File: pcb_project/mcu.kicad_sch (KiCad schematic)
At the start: 0 parts

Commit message: Initial MCU schematic
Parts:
- added C28: 4.7μF, symbol Device:C
- added C29, C32: 1μF, symbol Device:C
- added C30, C31, C33, C35, C36, C37, C38, C39: 100nF, symbol Device:C
- added C34, C41: 10pF, symbol Device:C
- added C40: 10μF, symbol Device:C
- added J3: Conn_ST_STDC14, symbol Connector:Conn_ST_STDC14
- added R46, R47, R48, R49: 47, symbol Device:R
- added SW1: SW_SPST, symbol Switch:SW_SPST
- added U4: STM32U595VJTx, Package_QFP:LQFP-100_14x14mm_P0.5mm, symbol MCU_ST_STM32U5:STM32U595VJTx
- added Y2: 48MHz, symbol Device:Crystal_GND24
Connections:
- new net: J3.10 (JTDI/NC), R47.1
- new net: R47.2, U4.77 (PA15)
- new net: C28.1, U4.48 (VCAP)
- new net: C41.1, U4.13 (PH1), Y2.3
- new net: C34.1, U4.12 (PH0), Y2.1
- new net: J3.8 (JTDO/SWO), R46.1
- new net: R46.2, U4.89 (PB3)
- new net: J3.12 (~{RST}), SW1.1 (A), U4.14 (NRST)
- new net: R49.2, U4.72 (PA13)
- new net: R48.2, U4.76 (PA14)
- new net: J3.4 (JTMS/SWDIO), R49.1
- new net: J3.6 (JCLK/SWCLK), R48.1
- new net +3V3: C29.1, C30.1, C31.1, C32.1, C33.1, C35.1, C36.1, C37.1, C38.1, C39.1, C40.1, J3.3 (VCC), U4.100 (VDD), U4.11 (VDD), U4.21 (VREF+), U4.22 (VDDA), U4.28 (VDD), U4.50 (VDD), U4.6 (VBAT), U4.73 (VDDUSB), U4.75 (VDD)
- new net GND: C28.2, C29.2, C30.2, C31.2, C32.2, C33.2, C34.2, C35.2, C36.2, C37.2, C38.2, C39.2, C40.2, C41.2, J3.5 (GND), J3.7 (GND), SW1.2 (B), U4.10 (VSS), U4.19 (VSSA), U4.20 (VREF-), U4.27 (VSS), U4.49 (VSS), U4.74 (VSS), U4.99 (VSS), Y2.2, Y2.4
- no-connect marks 0 -> 4
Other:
- note added: "VDD"
- note added: "VDDA"
- note added: "VDDUSB"
- note added: "VREF+ ??"

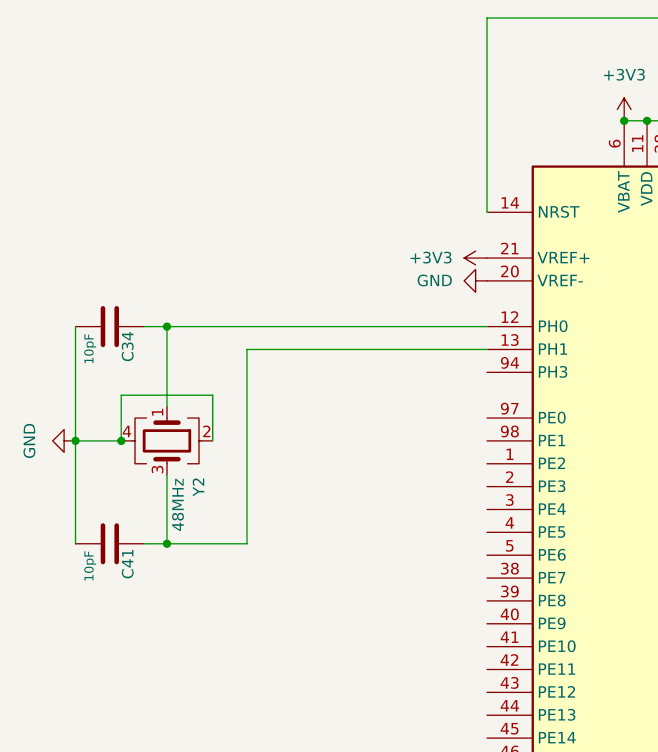
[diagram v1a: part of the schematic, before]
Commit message: Add switch for MCU BOOT pin
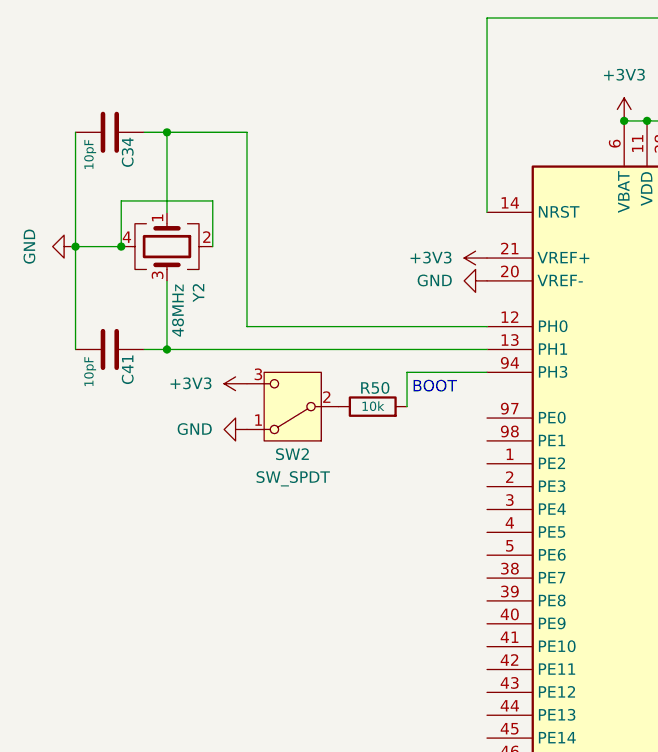
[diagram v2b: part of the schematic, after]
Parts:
- added R50: 10k, symbol Device:R
- added SW2: SW_SPDT, symbol Switch:SW_SPDT
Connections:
- net +3V3: now also SW2.3 (C)
- net GND: now also SW2.1 (A)
- net at U4.94 (PH3): now also R50.2
- new net: R50.1, SW2.2 (B)
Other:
- note added: "BOOT"
- moved on the sheet: C34, C41, Y2
